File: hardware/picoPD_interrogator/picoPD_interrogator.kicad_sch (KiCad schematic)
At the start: 25 parts, among them Q1 rohm-RE1C002UN, Q2 rohm-RE1C002UN, Q3 rohm-RE1C002UN, Q4 rohm-RE1C002UN, U2 ST-LM393QT

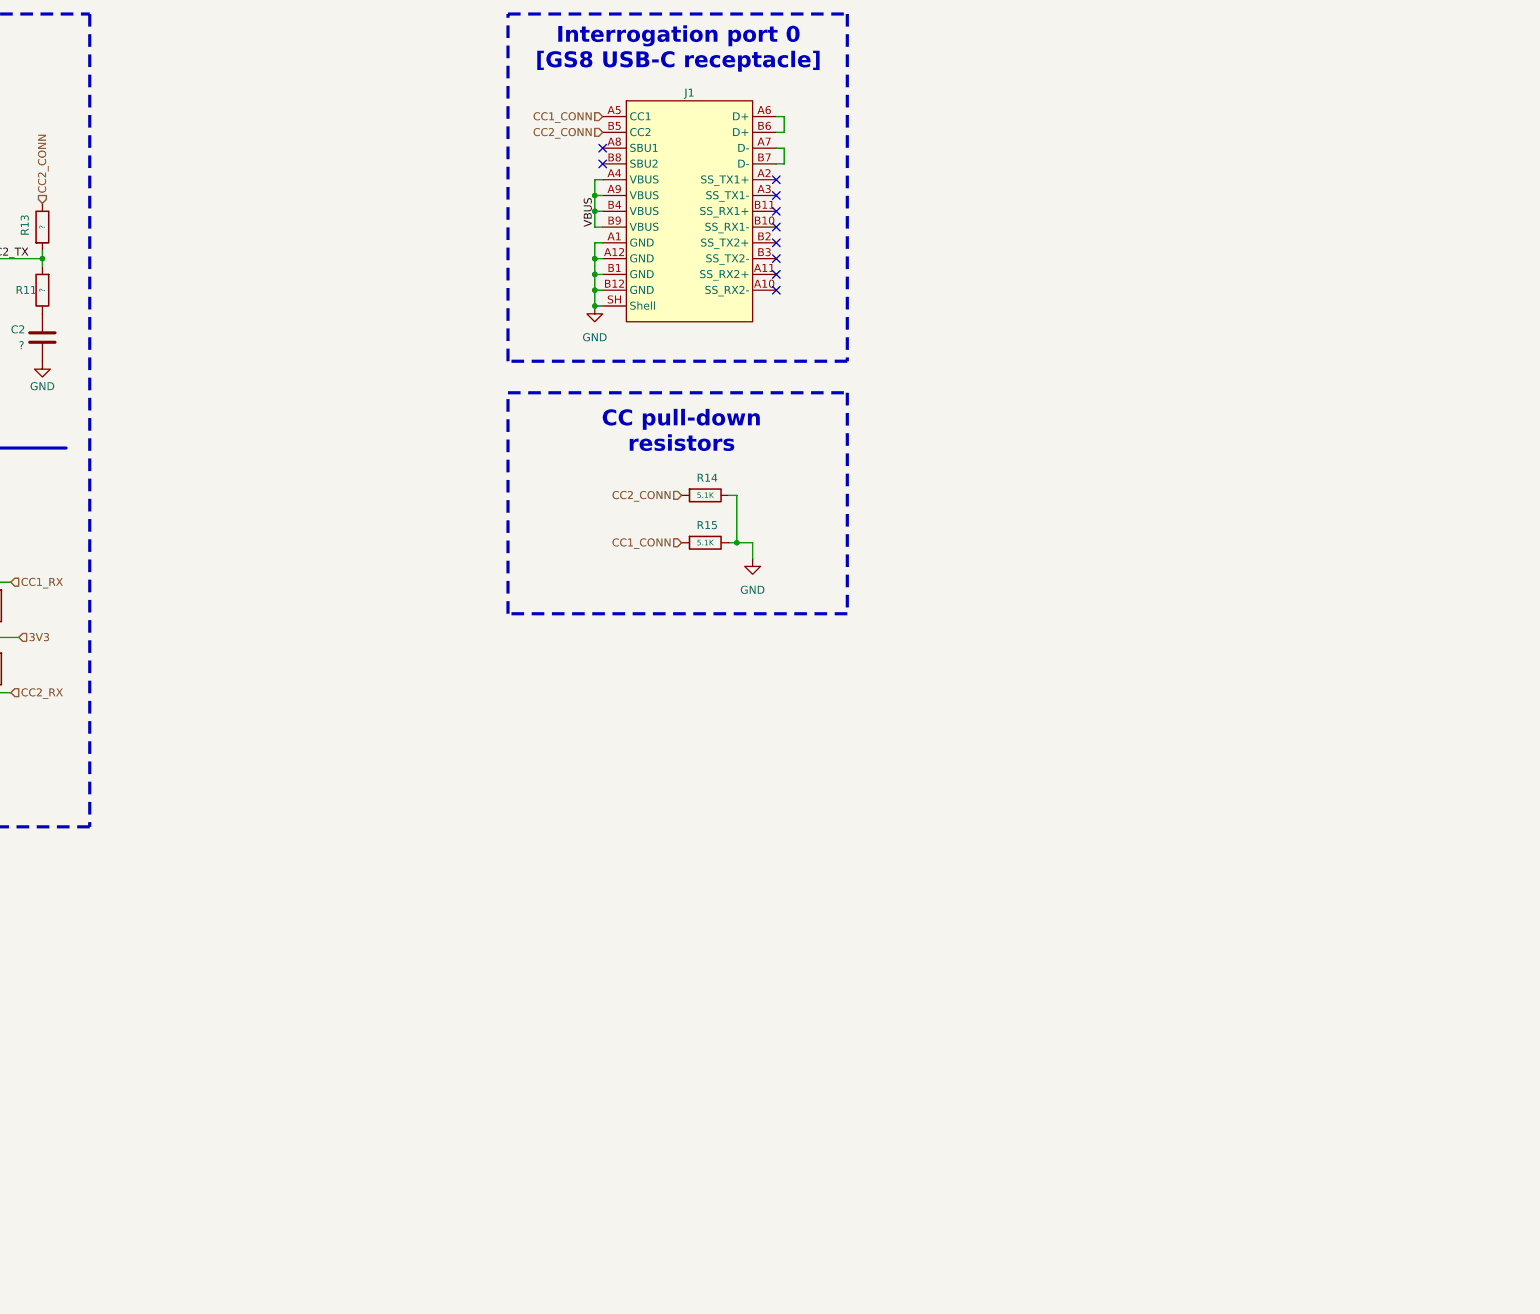
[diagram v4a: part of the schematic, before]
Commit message: Added DPDT switch for connector orientation & passthrough mode.
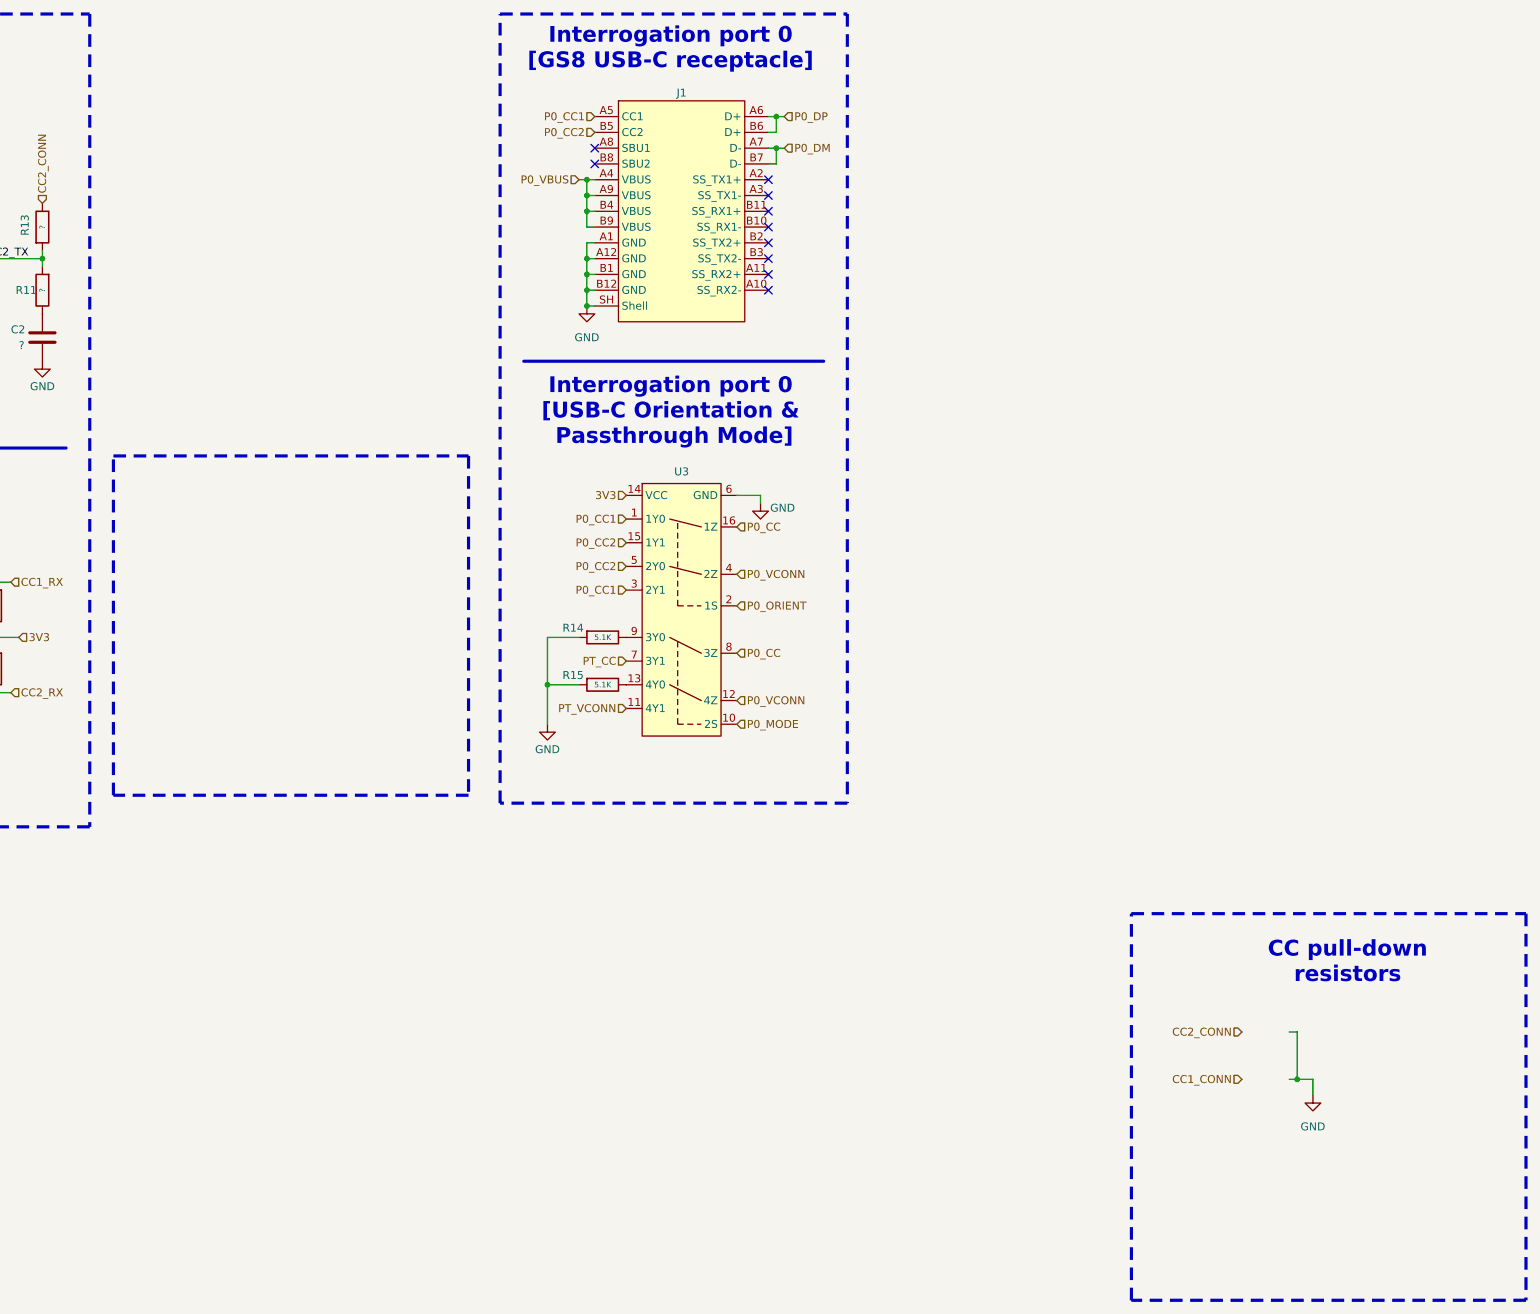
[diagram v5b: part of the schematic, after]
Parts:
- added U3: ~, symbol picoPD_interrogator:NXP_NX3DV3899GU
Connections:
- net 3V3: now also U3.14 (VCC)
- net CC1_CONN: no longer J1.A5 (CC1), R15.2
- net CC2_CONN: no longer J1.B5 (CC2), R14.2
- net GND: now also R14.2, R15.2, U3.6 (GND); no longer R14.1, R15.1
- net P0_DP: now reaches J1.A6 (D+), J1.B6 (D+)
- net P0_DM: now reaches J1.A7 (D-), J1.B7 (D-)
- net VBUS renamed P0_VBUS
- new net: R15.1, U3.13 (4Y0)
- new net: R14.1, U3.9 (3Y0)
- new net P0_CC: U3.16 (1Z), U3.8 (3Z)
- new net P0_CC1: J1.A5 (CC1), U3.1 (1Y0), U3.3 (2Y1)
- new net P0_CC2: J1.B5 (CC2), U3.15 (1Y1), U3.5 (2Y0)
- new net P0_MODE: U3.10 (2S)
- new net P0_ORIENT: U3.2 (1S)
- new net P0_VCONN: U3.12 (4Z), U3.4 (2Z)
- new net PT_CC: U3.7 (3Y1)
- new net PT_VCONN: U3.11 (4Y1)
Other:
- note added: "Interrogation port 0 [USB-C Orientation & Passthrough Mode]"
- moved on the sheet: J1, R14, R15

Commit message: Schematic: Added second interrogator port.
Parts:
- added J3: ~, picoPD_interrogator:USB-C_GS8, symbol picoPD_interrogator:USB-C_24pSH
- added R16, R17: 5.1K, Resistor_SMD:R_0201_0603Metric, symbol Device:R
- added U4: ~, symbol picoPD_interrogator:NXP_NX3DV3899GU
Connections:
- net CC1_CONN is gone; now on net P0_CC: R10.2, U1.31 (GP26_A0), U2.2 (-)
- net CC2_TX is gone; now on net P0_TX: Q3.2 (S), Q4.3 (D), R11.2, R13.2
- net 3V3: now also U4.14 (VCC)
- net GND: now also J3.A1 (GND), J3.A12 (GND), J3.B1 (GND), J3.B12 (GND), J3.SH (Shell), U4.6 (GND)
- net PT_CC: now also U4.7 (3Y1)
- net PT_VCONN: now also U4.11 (4Y1)
- net CC1_RX renamed P0_CC_RX
- net CC1_TX renamed P0_TX
- net CC1_TX_H renamed P0_TX_H
- net CC1_TX_L renamed P0_TX_L
- net CC2_CONN renamed P1_CC
- net P1_CC: now also U4.16 (1Z), U4.8 (3Z)
- net CC2_RX renamed P1_CC_RX
- net CC2_TX_H renamed P1_TX_H
- net CC2_TX_L renamed P1_TX_L
- new net: R16.1, U4.9 (3Y0)
- new net: R16.2, R17.2
- new net: R17.1, U4.13 (4Y0)
- new net P1_CC1: J3.A5 (CC1), U4.1 (1Y0), U4.3 (2Y1)
- new net P1_CC2: J3.B5 (CC2), U4.15 (1Y1), U4.5 (2Y0)
- new net P1_DM: J3.A7 (D-), J3.B7 (D-)
- new net P1_DP: J3.A6 (D+), J3.B6 (D+)
- new net P1_MODE: U4.10 (2S)
- new net P1_ORIENT: U4.2 (1S)
- new net P1_VBUS: J3.A4 (VBUS), J3.A9 (VBUS), J3.B4 (VBUS), J3.B9 (VBUS)
- new net P1_VCONN: U4.12 (4Z), U4.4 (2Z)
- no-connect marks 40 -> 50
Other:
- note added: "Interrogation port 0 [JAE USB-C receptacle]"
- note added: "Interrogation port 1 [JAE USB-C receptacle]"
- note added: "Interrogation port 1 [USB-C Orientation & Passthrough Mode]"
- note removed: "Interrogation port 0 [GS8 USB-C receptacle]"
- moved on the sheet: C1, C2, J1, J2, Q1, Q2, Q3, Q4, R1, R10, R11, R12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

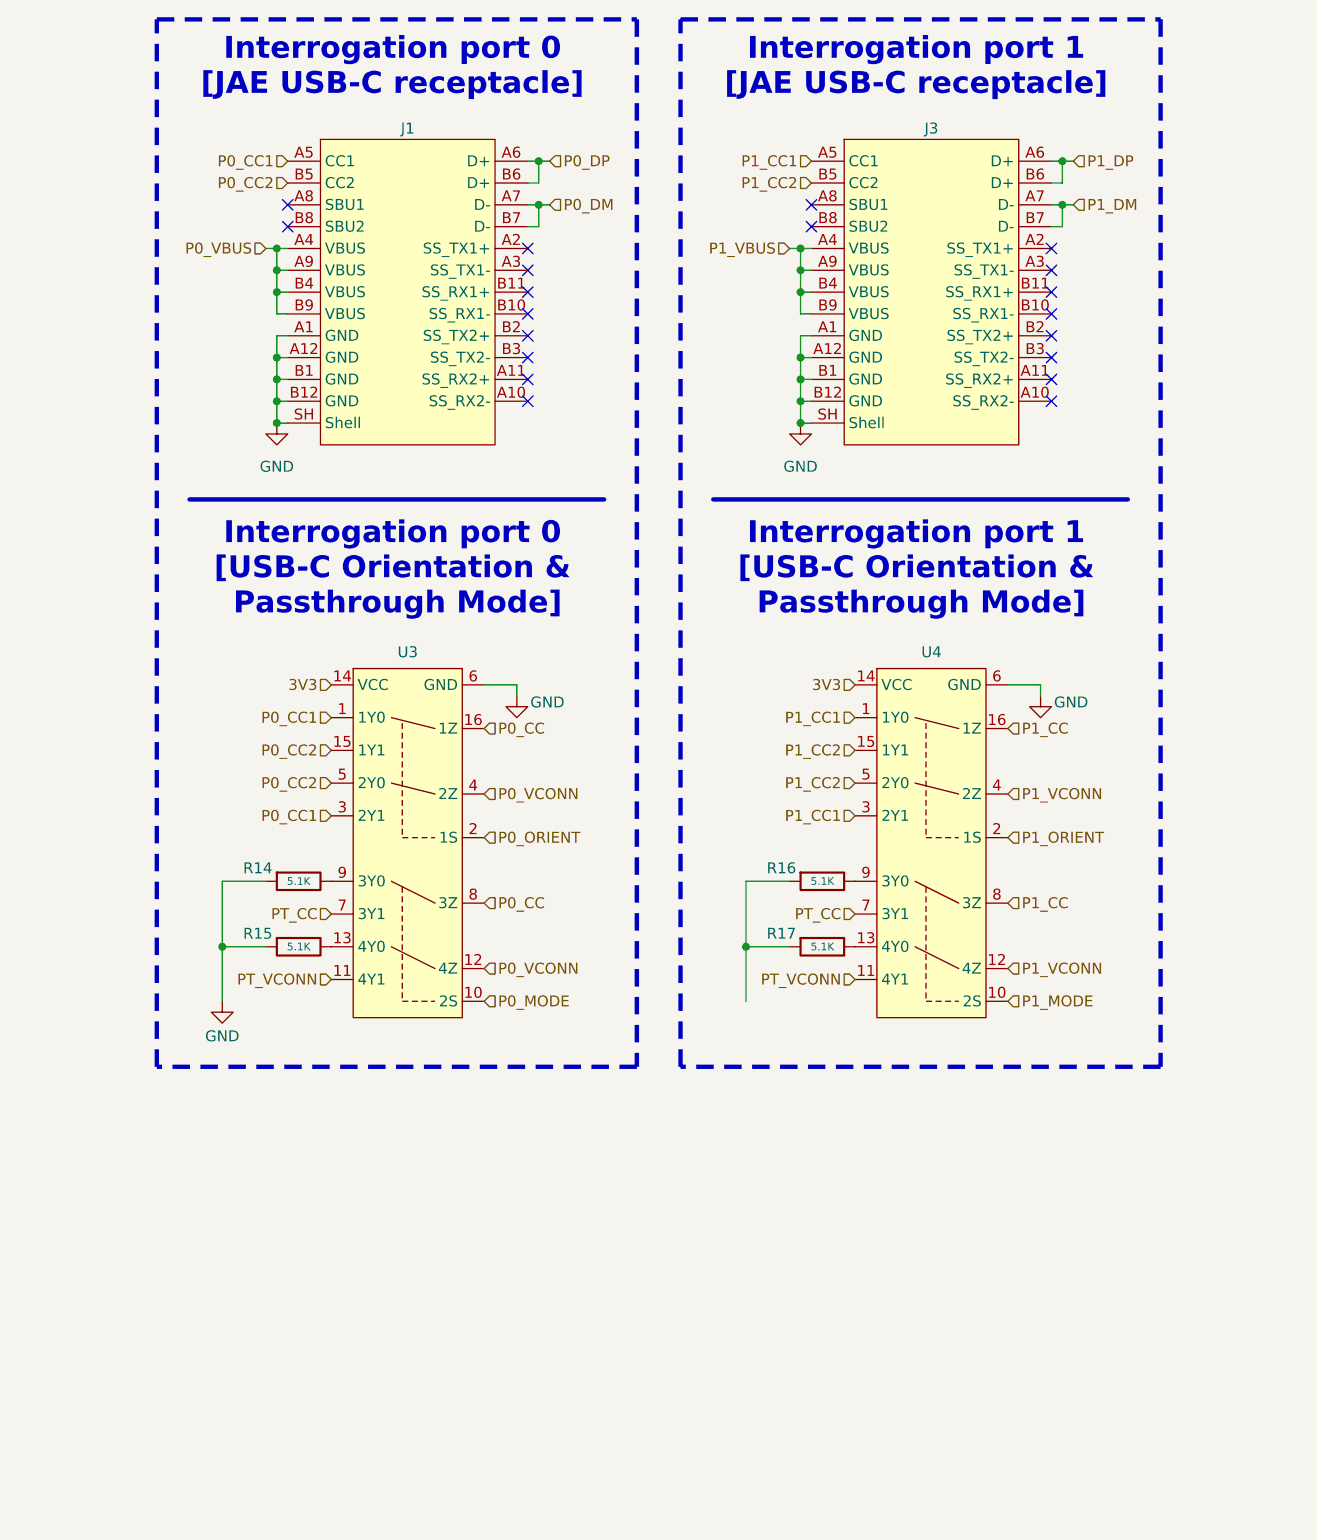
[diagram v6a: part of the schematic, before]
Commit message: Schematic: Added VCONN switches.
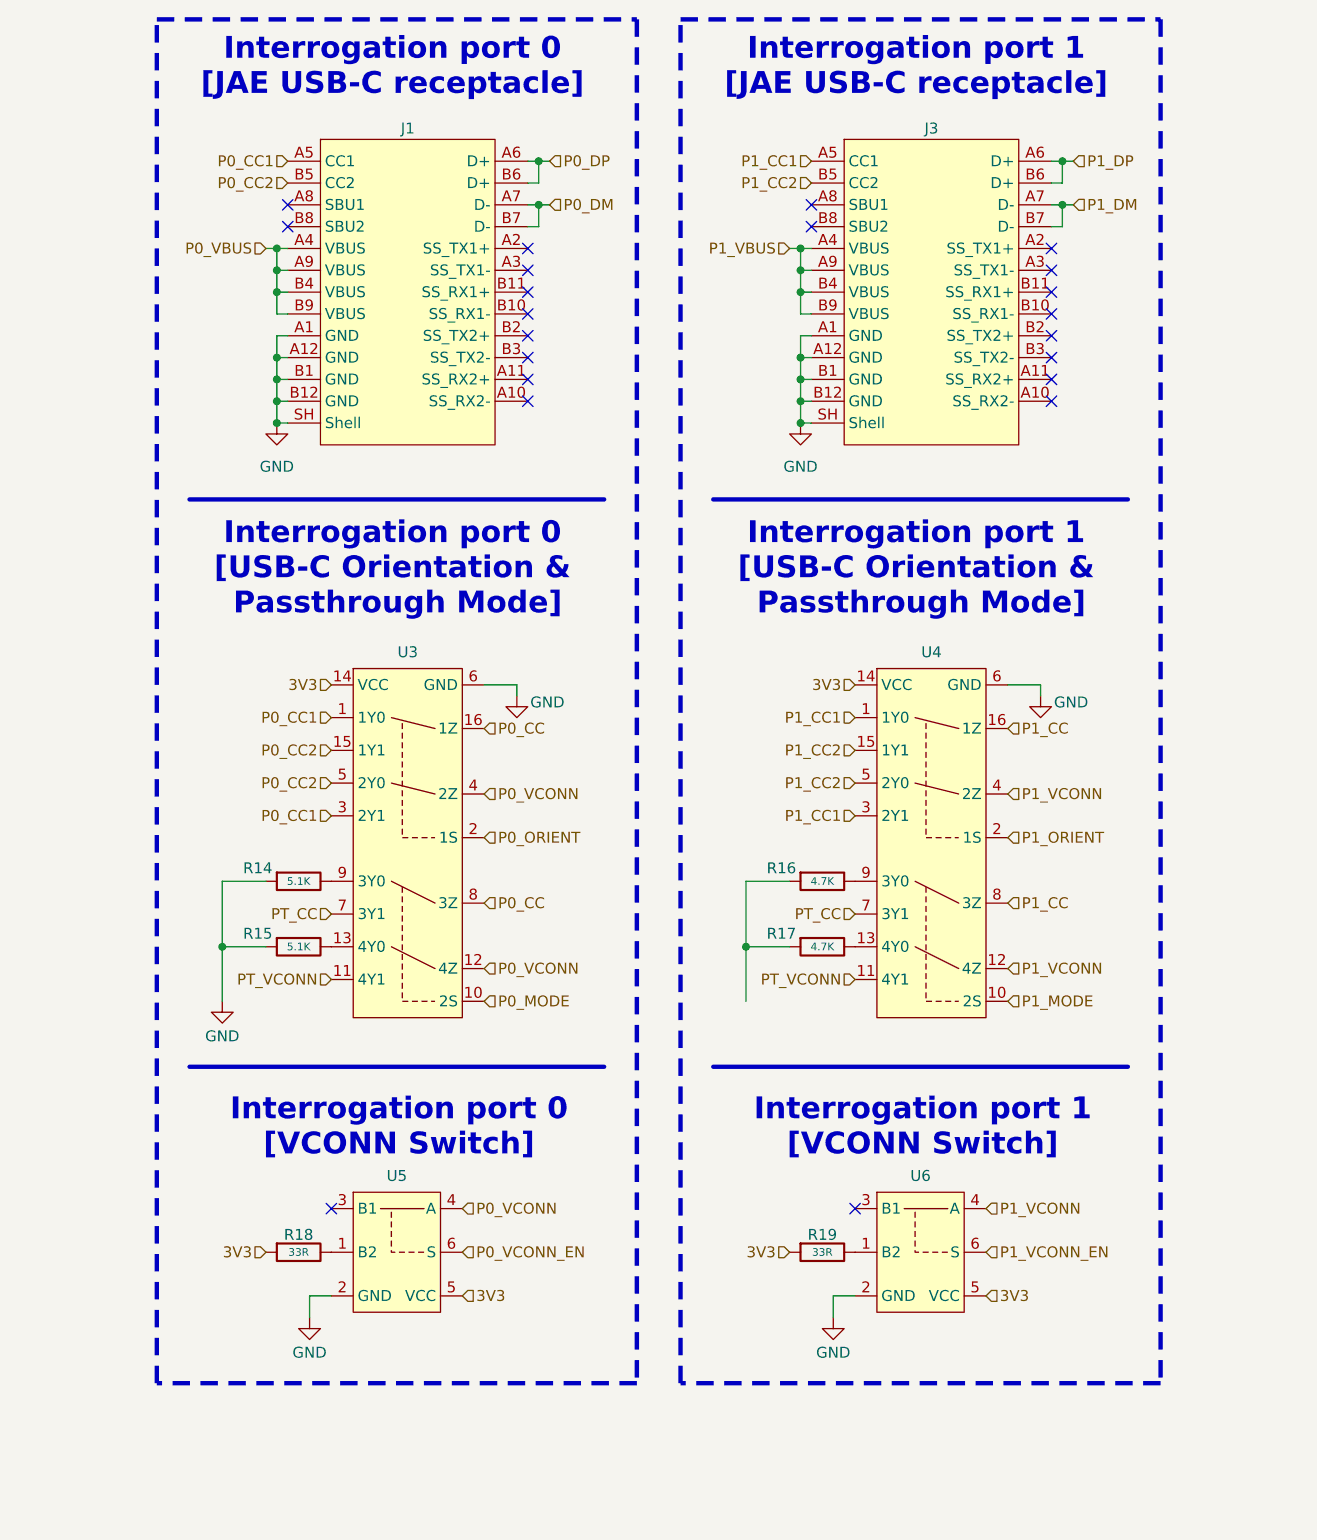
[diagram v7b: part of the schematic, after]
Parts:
- added R18, R19: 33R, Resistor_SMD:R_0201_0603Metric, symbol Device:R
- added U5, U6: ~, symbol picoPD_interrogator:TI_sn741vc1g3157-q1
- R16, R17: value 5.1K -> 4.7K
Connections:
- net 3V3: now also R18.2, R19.2, U5.5 (VCC), U6.5 (VCC)
- net GND: now also U5.2 (GND), U6.2 (GND)
- net P0_VCONN: now also U5.4 (A)
- net P1_VCONN: now also U6.4 (A)
- new net: R19.1, U6.1 (B2)
- new net: R18.1, U5.1 (B2)
- new net P0_VCONN_EN: U5.6 (S)
- new net P1_VCONN_EN: U6.6 (S)
- no-connect marks 50 -> 52
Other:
- note added: "Interrogation port 0 [VCONN Switch]"
- note added: "Interrogation port 1 [VCONN Switch]"
